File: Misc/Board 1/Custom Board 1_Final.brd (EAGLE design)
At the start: 101.6 x 78.8 mm, 54 parts, among them IC10 40193N, IC2 74LS595D, IC3 74LS595D, IC4 74LS595D, IC5 74LS595D, IC6 74LS595D, IC7 74LS595D, IC8 74AC11008, U1 AD9983AKSTZ_140, U2 SN54LS253_J_16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

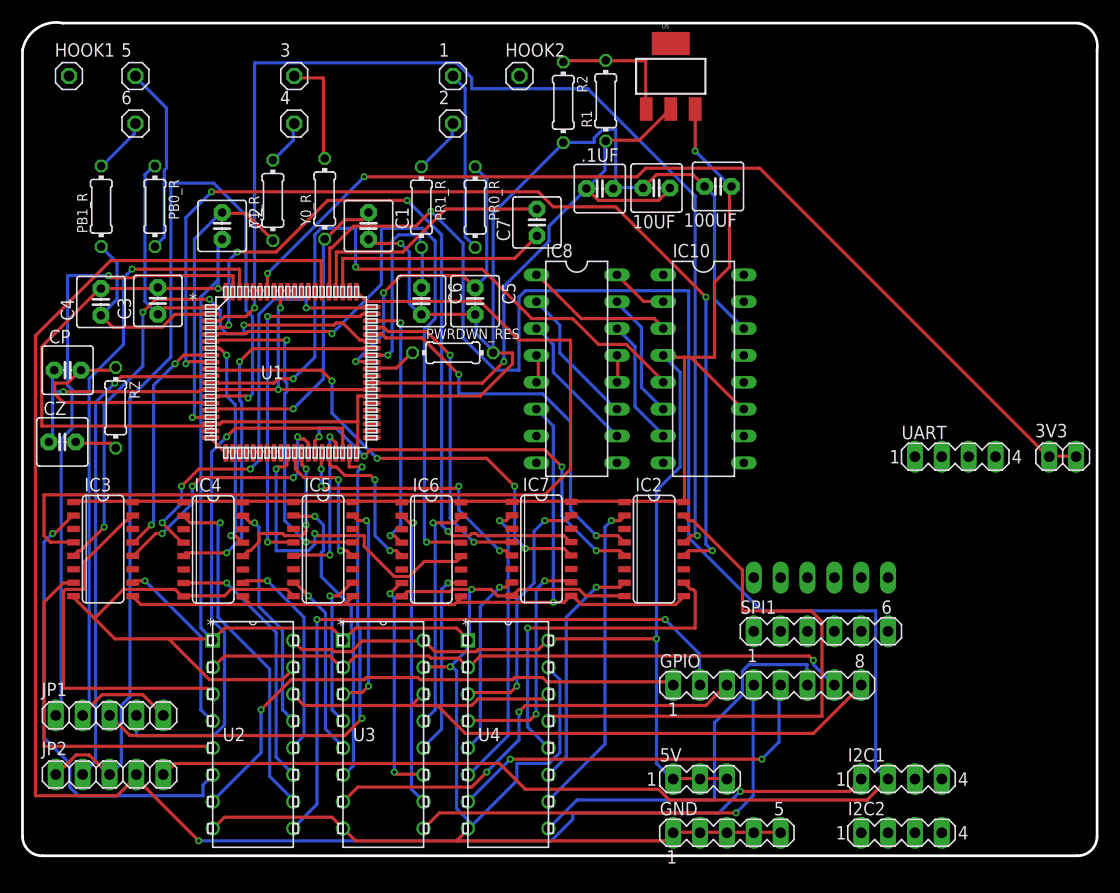
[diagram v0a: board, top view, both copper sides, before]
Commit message: Board Update Final
The board is wired (7 mil spacings, GND 21 mil, 18 mil power lines, and
12 mil regular lines), all spacings/special drill holes correct, ready
for fabrication
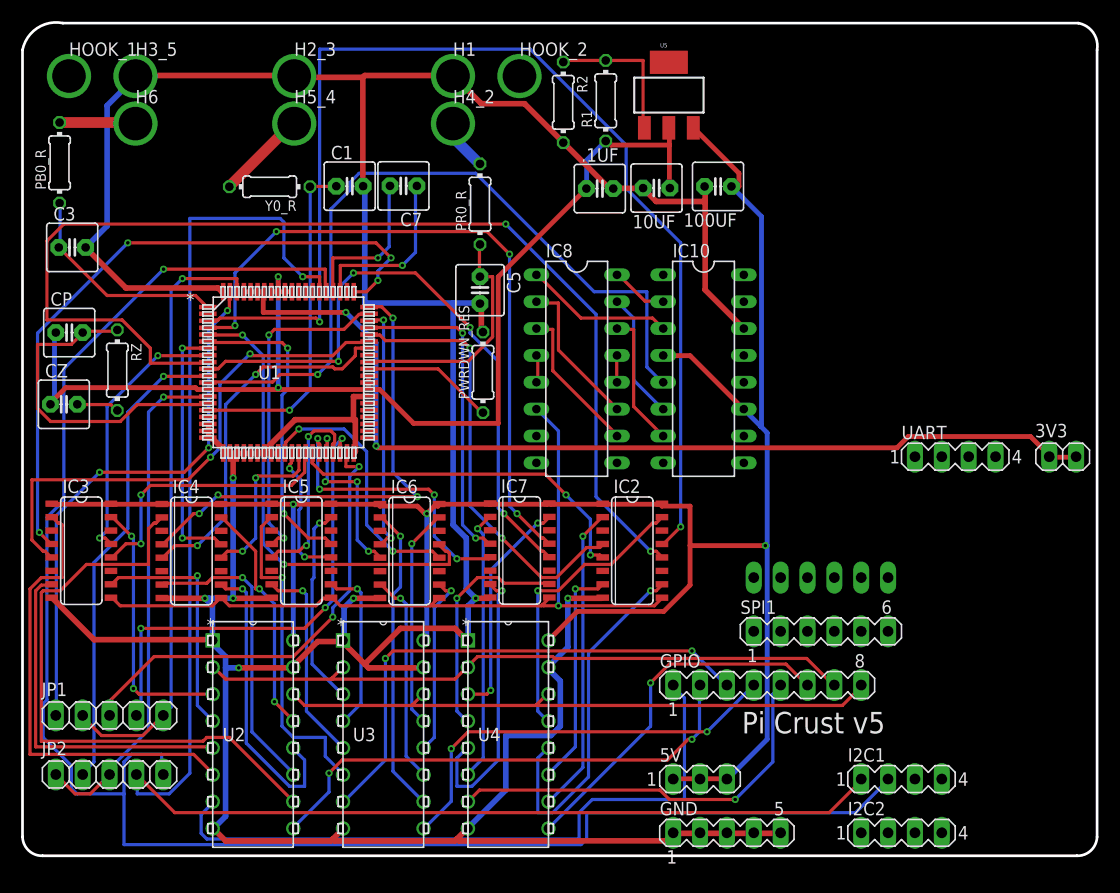
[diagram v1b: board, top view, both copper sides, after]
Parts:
- removed 1, 2, 3, 4, 5, 6, HOOK1, HOOK2: (no value), pinhead:1X01
- removed C2, C4, C6: (no value), capacitor-wima:C2.5-5
- removed PB1_R, PR1_R, Y1_R: (no value), eagle-ltspice:0204/7
- added H1, H2_3, H3_5, H4_2, H5_4, H6, HOOK_1, HOOK_2: SPECIAL_DRILL_0.1250, special-drill:PAD_0.1250
- moved C7 13.1 mm to (36.0, 63.3), turned to 180 degrees
- moved PB0_R 9.91 mm to (3.51, 65.5), turned to 90 degrees
- moved C3 9.55 mm to (4.70, 57.5), turned to 0 degrees
- moved Y0_R 5.33 mm to (23.4, 63.3), turned to 180 degrees
- moved C1 4.16 mm to (30.9, 63.3), turned to 0 degrees
- moved CZ 3.56 mm to (3.91, 42.7)
- moved RZ 3.56 mm to (8.97, 45.9)
- moved CP 3.56 mm to (4.42, 49.5)
- moved PWRDWN_RES 3.40 mm to (43.5, 45.7), turned to 90 degrees
- moved IC2 2.06 mm to (57.7, 28.9)
- moved IC6 2.06 mm to (36.6, 28.8)
- moved IC7 2.06 mm to (47.0, 28.9)
- moved IC3 2.06 mm to (5.56, 28.9)
- moved IC4 2.06 mm to (16.0, 28.8)
- moved IC5 2.06 mm to (26.4, 28.9)
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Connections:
- removed net PBIN_1: 6.1, PB1_R.2
- removed net PRIN_1: 2.1, PR1_R.1
- removed net YIN_1: 4.1, Y1_R.2
- net BIN1_ADC: no longer C4.1, PB1_R.1
- net GIN1_ADC: no longer C2.1, Y1_R.1
- net GND_WIRE: now also H1.1, H2_3.1, H3_5.1; no longer C2.2, C4.2, C6.2
- net PBIN_0: now also H6.1; no longer 5.1
- net PRIN_0: now also H4_2.1; no longer 1.1
- net RIN1_ADC: no longer C6.1, PR1_R.2
- net YIN_0: now also H5_4.1; no longer 3.1
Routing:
- net EXTCLK/COAST: track 94.7 -> 48.6 mm
- net R7: track 92.0 -> 63.5 mm, vias 0 -> 4
- net GIN1_ADC: track 28.3 -> 0.00 mm, vias 1 -> 0
- net B0_OUT: track 54.5 -> 27.4 mm, vias 0 -> 1
- net R6_OUT: track 33.2 -> 56.9 mm, vias 1 -> 0
- net SCL: track 189.7 -> 167.6 mm
- net RIN1_ADC: track 20.5 -> 0.00 mm, vias 1 -> 0
- net BIN1_ADC: track 19.1 -> 0.00 mm
- net GND_WIRE: track 413.5 -> 396.7 mm, vias 4 -> 7
- net B2: track 61.4 -> 44.6 mm
- net B7: track 46.1 -> 59.7 mm
- net MSB2: track 61.2 -> 47.7 mm
- net MSB1: track 51.2 -> 63.6 mm, vias 1 -> 0
- net PRIN_0: track 17.1 -> 4.89 mm
- net SDA: track 161.1 -> 149.5 mm, vias 2 -> 1
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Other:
- board text added: "Pi Crust v5"
- board text removed: "1.8V Power Supply"
- board text removed: "B"
- board text removed: "Connection to RPI1"
- board text removed: "Connection to RPI2"
- board text removed: "G"
- board text removed: "MUXs"
- board text removed: "R"
- board text removed: "RCJ-32"
- board text removed: "Row of DFF"
